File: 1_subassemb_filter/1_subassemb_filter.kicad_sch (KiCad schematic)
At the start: 59 parts, among them U1 X-opamp,IEEE, U10 X-opamp,IEEE, U11 X-opamp,IEEE, U12 X-opamp,IEEE, U13 X-opamp,IEEE, U14 X-opamp,IEEE, U2 X-opamp,IEEE, U3 X-opamp,IEEE, U4 X-opamp,IEEE, U5 X-opamp,IEEE, U6 X-opamp,IEEE, U7 X-opamp,IEEE, U8 X-opamp,IEEE, U9 X-opamp,IEEE

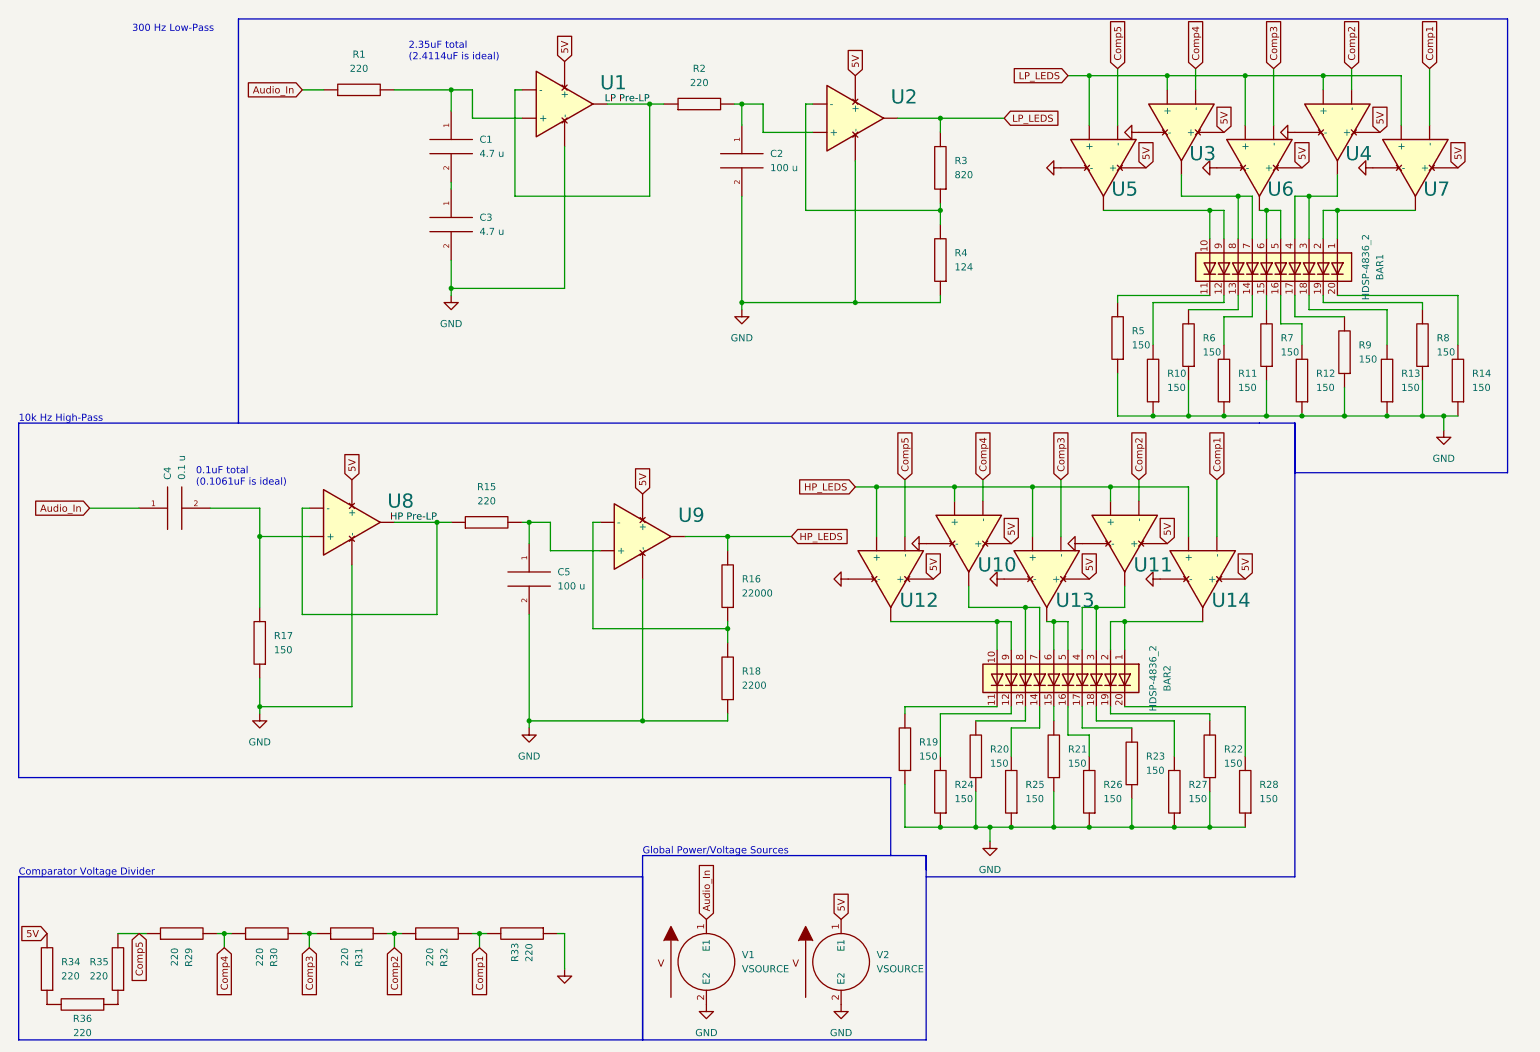
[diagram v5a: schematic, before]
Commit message: Updated with values from the breadboard
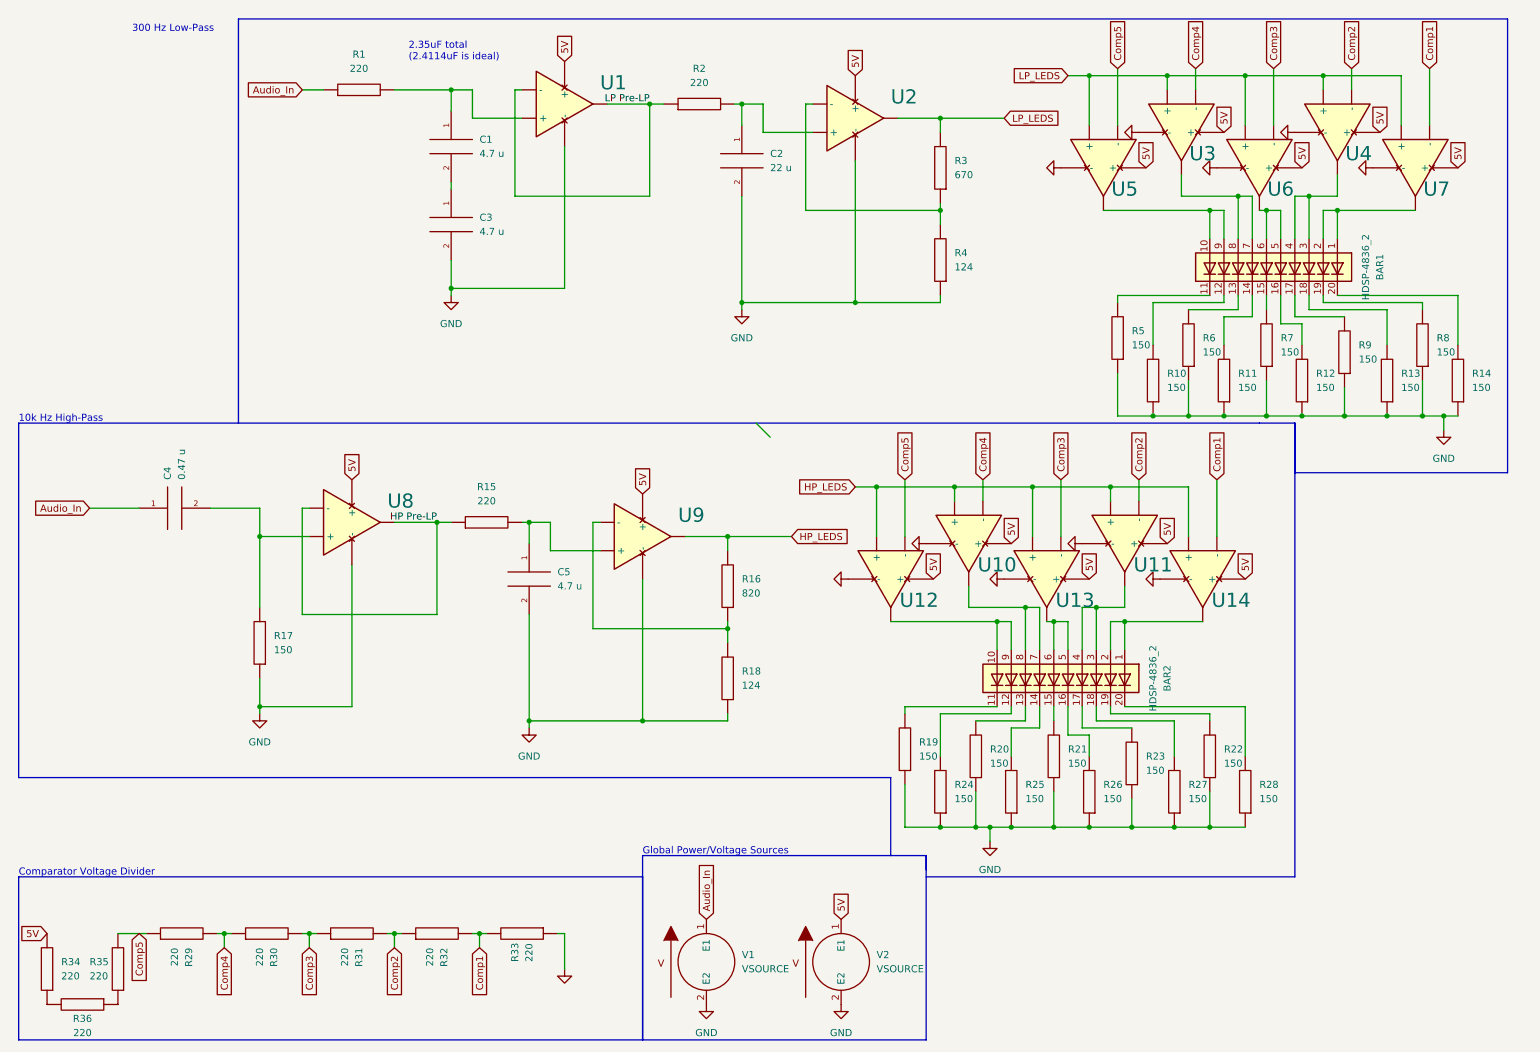
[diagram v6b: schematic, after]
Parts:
- C2: value 100 u -> 22 u
- C4: value 0.1 u -> 0.47 u
- C5: value 100 u -> 4.7 u
- R16: value 22000 -> 820
- R18: value 2200 -> 124
- R3: value 820 -> 670
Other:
- note removed: "0.1uF total (0.1061uF is ideal)"
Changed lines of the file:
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@@
   (junction (at 205.74 157.48) (diameter 0) (color 0 0 0 0)
+  )
+  (bus_entry (at 146.05 85.09) (size 2.54 2.54)
+    (stroke (width 0) (type default) (color 0 0 0 0))
   )
   (wire (pts (xy 127 27.94) (xy 129.54 27.94))
@@
   )
   (text "10k Hz High-Pass" (at 13.97 85.09 0)
-    (effects (font (size 1.27 1.27)) (justify left bottom))
-  )
-  (text "0.1uF total\n(0.1061uF is ideal)" (at 45.72 96.52 0)
     (effects (font (size 1.27 1.27)) (justify left bottom))
   )
@@
       (effects (font (size 1.27 1.27)) (justify left))
     )
-    (property "Value" "0.1 u" (id 1) (at 43.1799 95.25 0)
+    (property "Value" "0.47 u" (id 1) (at 43.1799 95.25 0)
       (effects (font (size 1.27 1.27)) (justify left))
     )
@@
       (effects (font (size 1.27 1.27)) (justify left))
     )
-    (property "Value" "100 u" (id 1) (at 148.59 39.37 0)
+    (property "Value" "22 u" (id 1) (at 148.59 39.37 0)
       (effects (font (size 1.27 1.27)) (justify left))
     )
@@
       (effects (font (size 1.27 1.27)) (justify right))
     )
-    (property "Value" "22000" (id 1) (at 143.51 115.5699 0)
+    (property "Value" "820" (id 1) (at 143.51 115.5699 0)
       (effects (font (size 1.27 1.27)) (justify right))
     )
@@
       (effects (font (size 1.27 1.27)) (justify left))
     )
-    (property "Value" "100 u" (id 1) (at 110.49 114.3 0)
+    (property "Value" "4.7 u" (id 1) (at 110.49 114.3 0)
       (effects (font (size 1.27 1.27)) (justify left))
     )
@@
       (effects (font (size 1.27 1.27)) (justify right))
     )
-    (property "Value" "2200" (id 1) (at 143.51 132.0799 0)
+    (property "Value" "124" (id 1) (at 143.51 132.0799 0)
       (effects (font (size 1.27 1.27)) (justify right))
     )
@@
       (effects (font (size 1.27 1.27)) (justify right))
     )
-    (property "Value" "820" (id 1) (at 181.61 40.6399 0)
+    (property "Value" "670" (id 1) (at 181.61 40.6399 0)
       (effects (font (size 1.27 1.27)) (justify right))
     )
@@
     )
     (path "/1d0eaa6c-640f-410c-9d6e-71eefe2b6587"
-      (reference "C2") (unit 1) (value "100 u") (footprint "")
+      (reference "C2") (unit 1) (value "22 u") (footprint "")
     )
     (path "/86fa38b5-e636-45c7-865a-8e83980b13a9"
@@
     )
     (path "/0a2865ac-0981-4ab0-82e0-17ed9181d443"
-      (reference "C4") (unit 1) (value "0.1 u") (footprint "")
+      (reference "C4") (unit 1) (value "0.47 u") (footprint "")
     )
     (path "/df12d1cb-221b-4f8f-9a7d-21930b715f8e"
-      (reference "C5") (unit 1) (value "100 u") (footprint "")
+      (reference "C5") (unit 1) (value "4.7 u") (footprint "")
     )
     (path "/fd68268c-e37c-4e5c-adcd-1315ac79b90f"
@@
     )
     (path "/ed53fb8b-ae79-40cd-a939-1b03befcb068"
-      (reference "R3") (unit 1) (value "820") (footprint "")
+      (reference "R3") (unit 1) (value "670") (footprint "")
     )
     (path "/cd5f96ae-2d73-4da9-b938-c3a4b528330a"
@@
     )
     (path "/32a5ff4f-5ba1-4eea-8fba-e3941a3149fd"
-      (reference "R16") (unit 1) (value "22000") (footprint "")
+      (reference "R16") (unit 1) (value "820") (footprint "")
     )
     (path "/421feea1-1821-466e-9aac-666207150bf7"
@@
     )
     (path "/e2e530a3-e293-4e4f-85af-8d74ff1d540e"
-      (reference "R18") (unit 1) (value "2200") (footprint "")
+      (reference "R18") (unit 1) (value "124") (footprint "")
     )
     (path "/f412172e-90fa-4d77-89e1-cd3f69a8e009"

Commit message: Now including band-pass, all circuits prototyped and proven to work
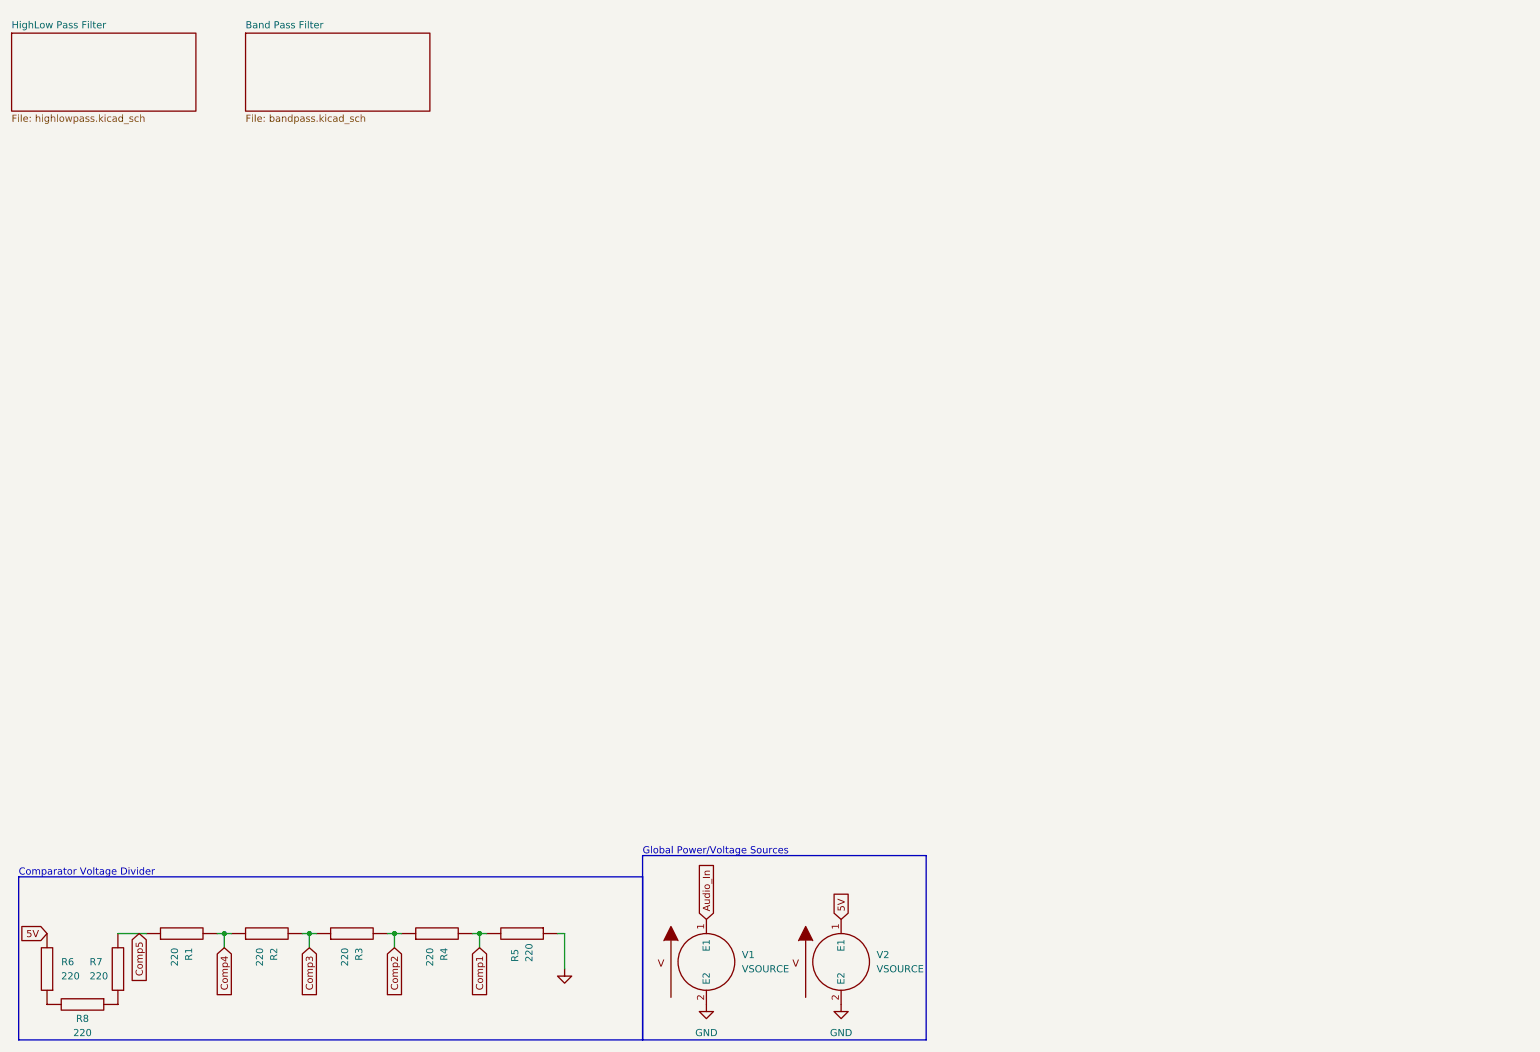
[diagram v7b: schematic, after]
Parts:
- removed BAR1, BAR2: HDSP-4836_2, Display:HDSP-4836, symbol LED:HDSP-4836_2
- removed C1, C3, C5: 4.7 u, symbol pspice:C
- removed C2: 22 u, symbol pspice:C
- removed C4: 0.47 u, symbol pspice:C
- removed R1, R15, R2: 220, symbol pspice:R
- removed R10, R11, R12, R13, R14, R17, R19, R20, R21, R22, R23, R24, R25, R26, R27, R28, R5, R6, R7, R8, R9: 150, symbol pspice:R
- removed R16: 820, symbol pspice:R
- removed R18, R4: 124, symbol pspice:R
- removed R3: 670, symbol pspice:R
- removed U1, U10, U11, U12, U13, U14, U2, U3, U4, U5, U6, U7, U8, U9: X-opamp,IEEE, symbol Generic:X-opamp,IEEE
- renumbered R29 to R1, R30 to R2, R31 to R3, R32 to R4, R33 to R5, R34 to R6, R35 to R7, R36 to R8
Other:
- added sheet Band Pass Filter (bandpass.kicad_sch)
- added sheet HighLow Pass Filter (highlowpass.kicad_sch)
- note removed: "10k Hz High-Pass"
- note removed: "2.35uF total (2.4114uF is ideal)"
- note removed: "300 Hz Low-Pass"
- title: Low/High-Pass Filters with Bar Graph LEDs -> Pass Filters with Bar Graph LEDs
